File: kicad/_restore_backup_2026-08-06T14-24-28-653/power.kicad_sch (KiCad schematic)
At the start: 19 parts, among them J4 2.1mm ID 5.5mm OD PJ-102AH, Q1 DMP3013SFV, U10 TLV75733PDBV, U11 TLV75733PDBV, U9 TPS62163DSG

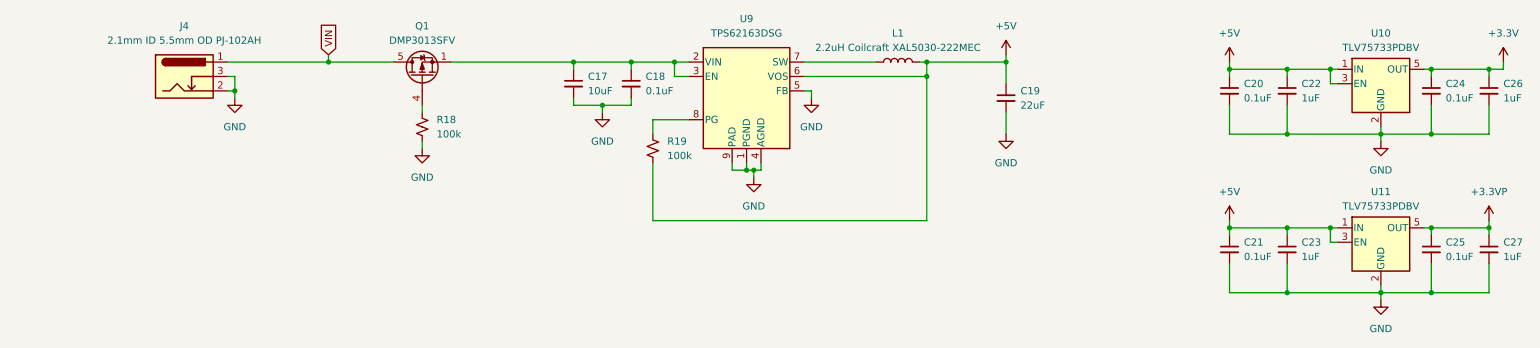
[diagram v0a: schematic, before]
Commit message: fix silkscreen
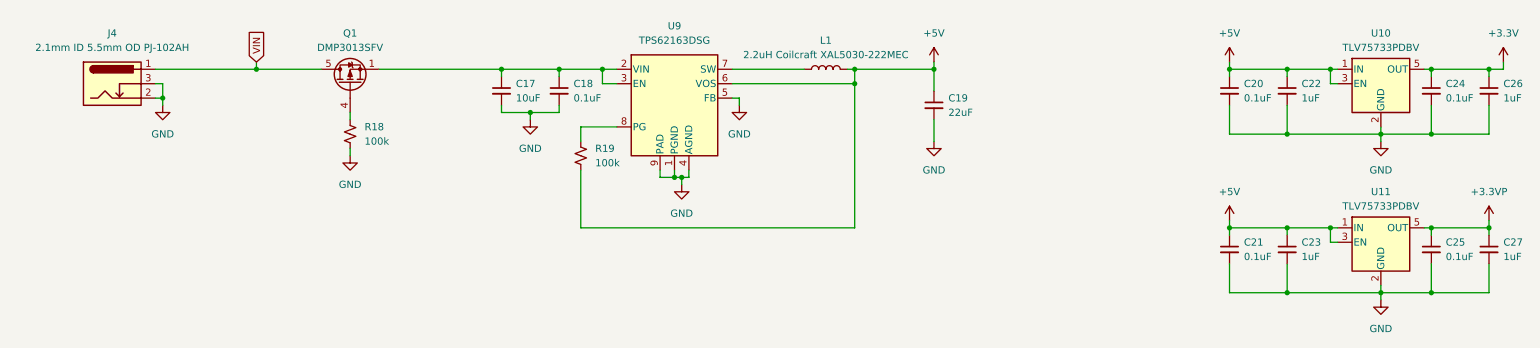
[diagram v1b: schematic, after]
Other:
- moved on the sheet: C17, C18, C19, J4, L1, Q1, R18, R19, U9
